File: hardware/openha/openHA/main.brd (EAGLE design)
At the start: 20 x 20 mm, 58 parts, among them U1 STM32L476JX, U2 PCM1774RGPR, U3 STC3115IQT, X1 ABS06-107SMT, X2 ABS06-107SMT

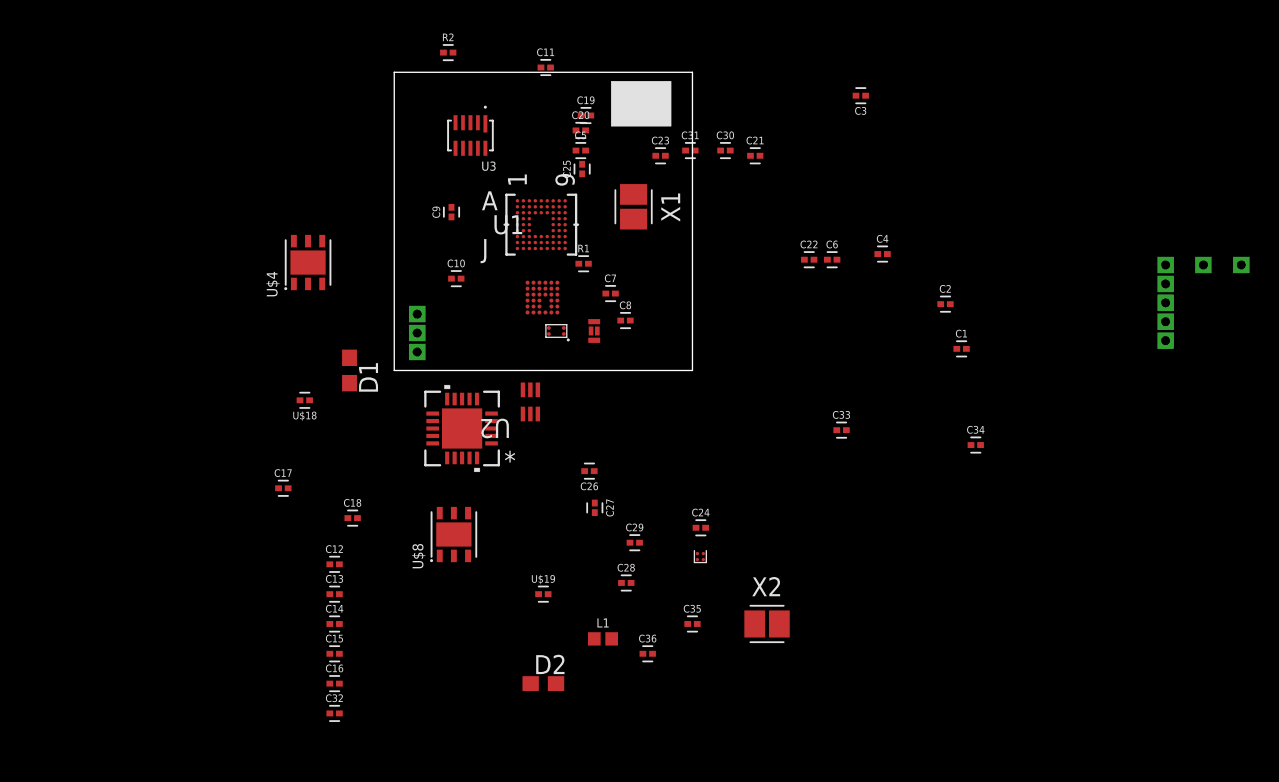
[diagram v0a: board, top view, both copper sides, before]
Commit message: Initial corrections
Miscellaneous corrections of the initial commit
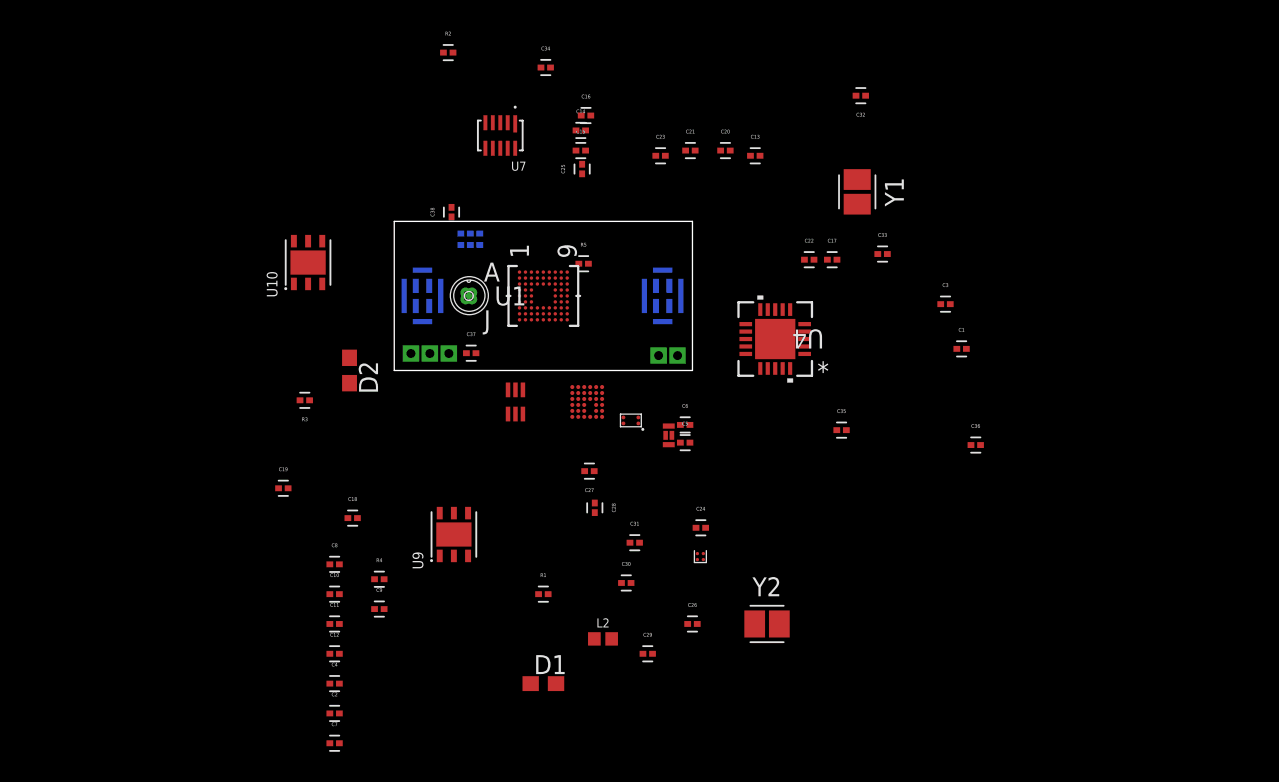
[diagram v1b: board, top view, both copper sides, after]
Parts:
- removed U$1: BATT, STM32:BATCONN
- removed U$15: BLUENRG-MS, STM32:WLCSP34
- removed U$16: BALF-NRG-01D3, STM32:FLIPCHIP
- removed U$17: ANT, STM32:ANTPACK
- removed U$18, U$19: 2k, STM32:CAPC0603X30
- removed U$2: USB, STM32:USB-MICRO-DUMMY
- removed U$3: LD5115J18, STM32:FLIPCHIP-2
- removed U$4: STBC08, STM32:DFN6
- removed U$5: USBLC6-2, STM32:SOT-666
- removed U$7: MP34DT05-A, STM32:MIC-PACK
- removed U$8: LDK130, STM32:DFN6
- removed X1, X2: ABS06-107SMT, STM32:CAPC2215X70
- added A1: ANT, OAlib:ANTPACK
- added C37, C38: 4.7uF, OAlib:CAPC0603X30
- added J1: 2PIN, OAlib:2PINCON
- added J2: BATT, OAlib:BATCONN
- added J3: CS44, OAlib:CS44
- added L2: 3.9NH, SparkFun-Coils:0402
- added R3: 2k, OAlib:CAPC0603X30
- added R4: 0R, OAlib:CAPC0603X30
- added R5: 20k, OAlib:CAPC0603X30
- added S2: SW_DPDT, OAlib:SW_DPDT
- added U10: STBC08, OAlib:DFN6
- added U4: PCM1774RGPR, PCM1774:RGP20_2P7X2P7
- added U5: BLUENRG-MS, OAlib:WLCSP34
- added U6: LD39115J18, OAlib:FLIPCHIP-2
- added U7: STC3115IQT, STC3115IQT:SON50P300X200X60-10N
- added U8: USBLC6-2, OAlib:SOT-666
- added U9: LDK130, OAlib:DFN6
- added Y1, Y2: ABS06-107SMT, OAlib:CAPC2215X70
- C1, C11, C12, C17, C18, C19, C21, C22, C23, C24, C25, C3, C7, C8, R2: device STM32:CAPC0603X30 -> OAlib:CAPC0603X30
- C10, C34, C6, C9: value 4.7uF -> 1uF; device STM32:CAPC0603X30 -> OAlib:CAPC0603X30
- C13: value 1uF -> 100nF; device STM32:CAPC0603X30 -> OAlib:CAPC0603X30
- C14, C15, C16: value 1uF -> 4.7uF; device STM32:CAPC0603X30 -> OAlib:CAPC0603X30
- C2: value 4pF -> 1uF; device STM32:CAPC0603X30 -> OAlib:CAPC0603X30
- C20: value 4.7uF -> 100pF; device STM32:CAPC0603X30 -> OAlib:CAPC0603X30
- C26: value 150nF -> 15pF; device STM32:CAPC0603X30 -> OAlib:CAPC0603X30
- C27: value 100p -> 150nF; device STM32:CAPC0603X30 -> OAlib:CAPC0603X30
- C28: value 100nF -> 100p; device STM32:CAPC0603X30 -> OAlib:CAPC0603X30
- C29: value 1uF -> 15pF; device STM32:CAPC0603X30 -> OAlib:CAPC0603X30
- C30: value 100pF -> 100nF; device STM32:CAPC0603X30 -> OAlib:CAPC0603X30
- C31, C4: value 100nF -> 1uF; device STM32:CAPC0603X30 -> OAlib:CAPC0603X30
- C32: value 1uF -> 4pF; device STM32:CAPC0603X30 -> OAlib:CAPC0603X30
- C33, C5: value 4.7uF -> 100nF; device STM32:CAPC0603X30 -> OAlib:CAPC0603X30
- C35, C36: value 15pF -> 4.7uF; device STM32:CAPC0603X30 -> OAlib:CAPC0603X30
- L1: value 3.9NH -> BALF-NRG-01D3; device SparkFun-Coils:0402 -> OAlib:FLIPCHIP
- R1: value 20k -> 2k; device STM32:CAPC0603X30 -> OAlib:CAPC0603X30
- U1: device STM32:WLCSP72 -> OAlib:WLCSP72
- U2: value PCM1774RGPR -> MP34DT05-A; device PCM1774:RGP20_2P7X2P7 -> OAlib:MIC-PACK
- U3: value STC3115IQT -> MP34DT05-A; device STC3115IQT:SON50P300X200X60-10N -> OAlib:MIC-PACK
- moved C32 54.4 mm to (31.3, 18.4), turned to 180 degrees
- moved C2 49.3 mm to (-4.00, -23.0)
- moved C4 46.7 mm to (-4.00, -21.0)
- moved C16 41.7 mm to (12.9, 17.1)
- moved C13 40.7 mm to (24.2, 14.4)
- moved C11 39.9 mm to (-4.00, -17.0)
- moved C17 39.9 mm to (29.4, 7.43)
- moved C34 38.4 mm to (10.2, 20.3)
- moved C15 37.6 mm to (12.5, 14.8)
- moved C14 37.0 mm to (12.5, 16.1)
- moved C7 35.4 mm to (-4.00, -25.0)
- moved C19 32.2 mm to (-7.44, -7.90)
- moved C30 29.8 mm to (15.6, -14.2)
- moved C9 27.1 mm to (-1.00, -16.0), turned to 0 degrees
- moved C31 26.6 mm to (16.1, -11.6)
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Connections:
- removed net GG_SCL: U3.3
- removed net GG_SDA: U1.G1, U3.2
- removed net GPIO2: U1.F8, U2.3
- removed net GPIO3: U1.F9, U2.4
- removed net MIC_CLK: U$7.CLK, U1.F7
- removed net MIC_DATA: U$7.DOUT, U1.B7
- removed net RXD-USB_DM: U$5.1
- removed net SAI_FS: U2.11
- removed net SAI_MCLK: U2.10
- removed net VDD: C12.1, C13.1, C14.1, C15.1, C16.1, C22.1, C23.1, C24.1, C25.1, C26.1, C27.1, C28.2, C29.2, C3.1, C30.1, C31.1, C32.1, C7.1, C8.1, U$15.A3, U$15.C1, U$15.D5, U$15.F3, U$3.B1, U$7.VDD, U1.A9, U1.B9, U1.G8, U1.H9, U1.J1, U1.J8
- new net 1V8: C10.1, C11.1, C12.1, C2.1, C20.1, C21.1, C22.1, C23.1, C24.1, C25.1, C27.1, C28.1, C30.2, C31.2, C32.1, C4.1, C5.1, C6.1, C7.1, C8.1, C9.1, U1.A9, U1.B9, U1.G8, U1.H9, U1.J1, U1.J8, U2.VDD, U3.VDD, U5.A3, U5.C1, U5.D5, U5.F3, U6.B1
- new net I2C_SCL: U1.F9, U4.4, U7.3
- new net I2C_SDA: U1.F8, U4.3, U7.2
- new net MIC1_CLK: U1.F7, U2.CLK
- new net MIC1_DATA: U1.B7, U2.DOUT
- new net MIC2_CLK: U1.G3, U3.CLK
- new net MIC2_DATA: U1.H3, U3.DOUT
- new net N$20: U1.D2
- new net SAI_BCK: U1.C4, U4.10
- new net SAI_LR: U1.B4, U4.11
- new net SWDCLK: S2.4, U1.B2
- new net SWDIO: S2.1, U1.C2
- new net TXD-USB_DM: U1.D1, U8.1
- new net USB_DM: S2.6, U8.6
- new net USB_DP: S2.3, U8.4
- net 3V3: now also C13.2, C14.2, C15.2, C16.2, C17.2, C36.1, R4.2, U4.1, U4.13, U4.16, U4.18, U4.6, U4.7, U9.6; no longer C19.2, C20.2, C21.2, C34.1, C5.2, C6.2, U$8.6, U2.1, U2.13, U2.16, U2.18, U2.6, U2.7
- net BAT_NTC: now also J2.2, U7.8; no longer U$1.P$2, U3.8
- net BLUE_CLK: now also U5.E1; no longer U$15.E1
- net BLUE_CS: now also U5.F2; no longer U$15.F2
- net BLUE_IRQ: now also U5.D2; no longer U$15.D2
- net BLUE_MISO: now also U5.F1; no longer U$15.F1
- net BLUE_MOSI: now also U5.E2; no longer U$15.E2
- net CHRG: now also D2.1, U10.3; no longer D1.1, U$4.3
- net GND: now also A1.RADIATOR, C11.2, C13.1, C14.1, C15.1, C16.1, C17.1, C20.2, C21.2, C28.2, C36.2, C37.2, C38.2, C5.2, C6.2, D1.1, J2.3, J3.GND, L1.A2, L2.2, R5.2, U10.4, U10.7, U2.GND, U2.GND1, U2.GND2, U2.GND3, U2.LR, U3.GND, U3.GND1, U3.GND2, U3.GND3, U3.LR, U4.12, U4.17, U4.2, U4.21, U4.8, U5.A1, U5.A2, U5.A4, U5.A5, U5.B1, U5.B2, U5.B3, U5.B4, U5.B5, U5.C2, U5.C3, U5.D3, U5.D4, U5.E3, U5.F4, U6.A1, U7.5, U8.2, U9.2; no longer C13.2, C14.2, C15.2, C16.2, C19.1, C20.1, C21.1, C30.2, C31.2, C34.2, C5.1, C6.1, D2.1, L1.2, R1.2, U$1.P$3, U$15.A1, U$15.A2, U$15.A4, U$15.A5, U$15.B1, U$15.B2, U$15.B3, U$15.B4, U$15.B5, U$15.C2, U$15.C3, U$15.D3, U$15.D4, U$15.E3, U$15.F4, U$16.A2, U$17.RADIATOR, U$2.P$6, U$2.P$7, U$3.A1, U$4.4, U$5.2, U$7.GND, U$7.GND1, U$7.GND2, U$7.GND3, U$7.LR, U$8.2, U2.12, U2.17, U2.2, U2.21, U2.8, U3.5
- net HPL: now also J1.1
- net HPR: now also C19.2, J1.2; no longer C17.2
- net N$1: now also R1.1, U1.A7; no longer U$19.1, U1.A6
- net N$10: now also C19.1, U4.14; no longer C17.1, U2.14
- net N$11: now also J3.3, S2.2; no longer U$2.P$3, U$5.4
- net N$12: now also A1.FEED, L1.A1; no longer U$16.A1, U$17.FEED
- net N$13: now also L1.B1, U5.C6; no longer U$15.C6, U$16.B1
- net N$14: now also L1.B2, U5.D6; no longer U$15.D6, U$16.B2
- net N$15: now also D1.2, R1.2; no longer D2.2, U$19.2
- net N$19: now also C30.1, C31.1, U5.F5; no longer C28.1, C29.1, U$15.F5
- net N$2: now also C29.2, L2.1; no longer C36.2, L1.1
- net N$3: now also U4.15; no longer U2.15
- net N$6: now also D2.2, R3.2; no longer D1.2, U$18.2
- net N$7: now also C34.2, U7.6; no longer C11.2, U3.6
- net N$8: now also R5.1, U10.5; no longer R1.1, U$4.5
- net N$9: now also J3.2, S2.5; no longer U$2.P$2, U$5.6
- net OSC_BLUE_IN: now also C26.1, U5.A6, Y2.1; no longer C35.1, U$15.A6, X2.1
- net OSC_BLUE_OUT: now also C29.1, U5.B6, Y2.2; no longer C36.1, U$15.B6, X2.2
- net OSC_IN: now also Y1.1; no longer X1.1
- net OSC_OUT: now also C3.1, Y1.2; no longer C2.1, X1.2
- net RESETN: now also U5.E4; no longer U$15.E4
- net RXD-USB_DP: now also U1.C1, U8.3; no longer U$5.3
- net SAI_SCK: now also U1.A4, U4.9; no longer U2.9
- net SAI_SD: now also U1.C5, U4.5; no longer U2.5
- net SMPSFILT1: now also U5.F6; no longer U$15.F6
- net SXTAL0: now also U5.E5; no longer U$15.E5
- net SXTAL1: now also U5.E6; no longer U$15.E6
- net TEST1: now also U5.D1; no longer U$15.D1
- net VBAT: now also C34.1, C35.1, C38.1, J2.1, U10.1, U6.A2, U6.B2, U7.10, U7.9, U9.1; no longer C11.1, C33.1, C9.1, U$1.P$1, U$3.A2, U$3.B2, U$4.1, U$8.1, U3.10, U3.9
- net VDDUSB: now also R4.1
- net V_USB: now also C33.1, C37.1, J3.VCC, R3.1, U10.6, U8.5; no longer C10.1, C4.1, U$18.1, U$2.P$1, U$4.6, U$5.5
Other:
- board size 20 x 20 mm -> 20 x 10 mm

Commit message: Various BOM update
Replace 4pin micro connector by USB (used for USB and SWD)
Update BOM for LED, Crystal, Self and 3V3 LDO
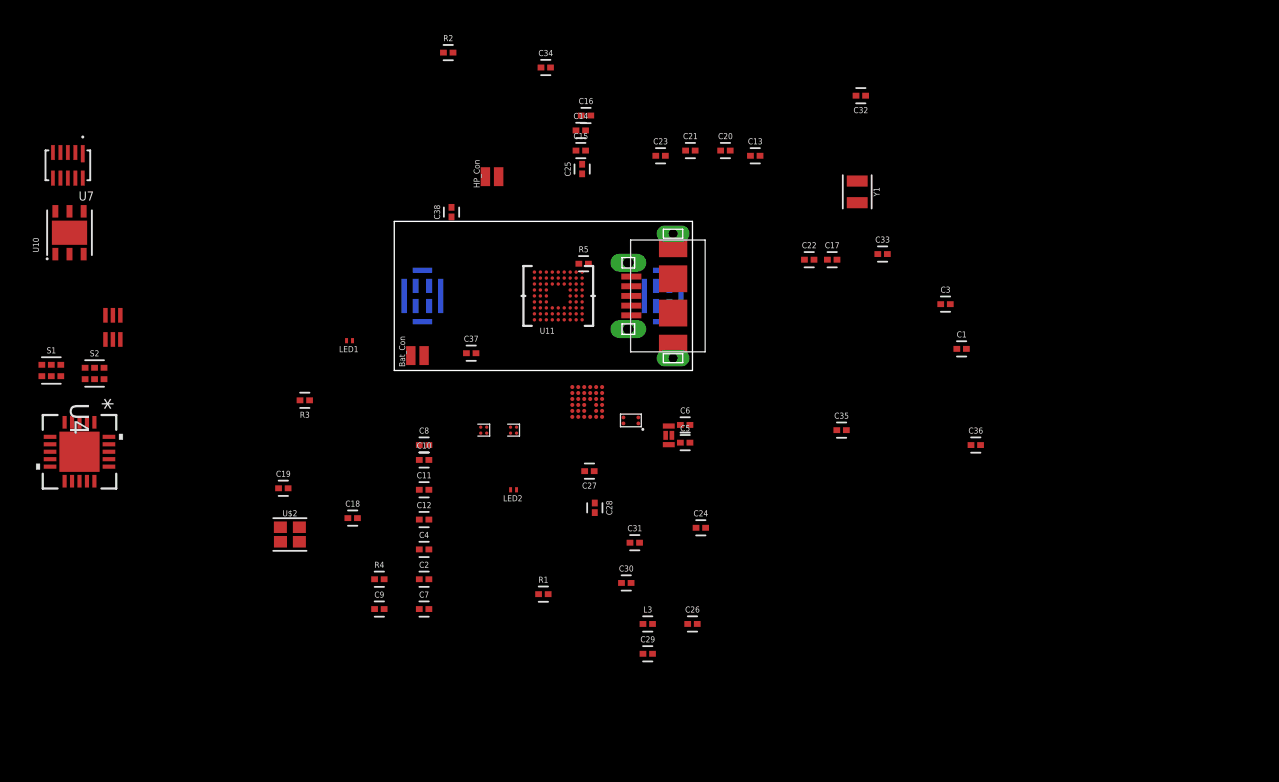
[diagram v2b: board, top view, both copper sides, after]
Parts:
- removed D1, D2: LTST-C191KSKT, LTST-C191KSKT:0603
- removed J2: BATT, OAlib:BATCONN
- removed L2: 3.9NH, SparkFun-Coils:0402
- removed U1: STM32L476JX, OAlib:WLCSP72
- removed Y2: ABS06-107SMT, OAlib:CAPC2215X70
- added L3: 3.9nH, OAlib:CAPC0603X30
- added LED1, LED2: (no value), OAlib:0.65X0.35X0.2MM(0201)SMDCHIPLE
- added S1: SW_DPDT, OAlib:SW_DPDT
- added U$1: MICRO-USB-RECEPTACLE47589-0001, OAlib:47589-0001
- added U$2: 32MHz, OAlib:ABM11W-101
- added U11: STM32L476JX, OAlib:WLCSP72
- J1: value 2PIN -> HP_Con
- J3: value CS44 -> Bat_Con; device OAlib:CS44 -> OAlib:2PINCON
- R2: value 50m -> 50M
- U6: value LD39115J18 -> LD39115J
- U9: value LDK130 -> LD39115J; device OAlib:DFN6 -> OAlib:FLIPCHIP-2
- Y1: value ABS06-107SMT -> 32.768kHz; device OAlib:CAPC2215X70 -> OAlib:ABS06-107
- moved U4 47.3 mm to (-21.1, -5.45), turned to 270 degrees
- moved U7 29.1 mm to (-21.9, 13.8)
- moved U8 27.5 mm to (-18.9, 2.89)
- moved S2 26.8 mm to (-20.1, -0.20), flipped to the top
- moved J1 17.0 mm to (7.00, 13.0)
- moved U6 16.8 mm to (6.00, -4.00), turned to 0 degrees
- moved U10 16.1 mm to (-21.8, 9.24)
- moved C10 10.8 mm to (2.00, -6.00)
- moved C11 10.8 mm to (2.00, -8.00)
- moved C12 10.8 mm to (2.00, -10.0)
- moved C2 10.8 mm to (2.00, -14.0)
- moved C4 10.8 mm to (2.00, -12.0)
- moved C7 10.8 mm to (2.00, -16.0)
- moved C8 10.0 mm to (2.00, -5.00)
- moved U9 8.06 mm to (8.00, -4.00), turned to 0 degrees
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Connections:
- removed net BAT_NTC: J2.2, U7.8
- new net N$16: S1.5, U$1.4
- new net SWDRST: S1.6, U11.E9
- net 1V8: now also U11.A9, U11.B9, U11.G8, U11.H9, U11.J1, U11.J8; no longer U1.A9, U1.B9, U1.G8, U1.H9, U1.J1, U1.J8
- net 3V3: now also U9.B1; no longer U9.6
- net BLUE_CLK: now also U11.H6; no longer U1.H6
- net BLUE_CS: now also U11.J3; no longer U1.J3
- net BLUE_IRQ: now also U11.J6; no longer U1.J6
- net BLUE_MISO: now also U11.H5; no longer U1.H5
- net BLUE_MOSI: now also U11.H4; no longer U1.H4
- net BLUE_RST: now also U11.D9; no longer U1.D9
- net CHRG: now also LED1.1; no longer D2.1
- net GND: now also J3.P$2, L3.2, LED2.1, U$1.5, U$2.2, U$2.4, U11.A8, U11.B1, U11.D7, U11.G9, U11.J2, U11.J9, U9.A1; no longer D1.1, J2.3, J3.GND, L2.2, U1.A8, U1.B1, U1.D7, U1.G9, U1.J2, U1.J9, U9.2
- net HPL: now also J1.P$1; no longer J1.1
- net HPR: now also J1.P$2; no longer J1.2
- net I2C_SCL: now also U11.F9; no longer U1.F9
- net I2C_SDA: now also U11.F8; no longer U1.F8
- net MIC1_CLK: now also U11.F7; no longer U1.F7
- net MIC1_DATA: now also U11.B7; no longer U1.B7
- net MIC2_CLK: now also U11.G3; no longer U1.G3
- net MIC2_DATA: now also U11.H3; no longer U1.H3
- net N$1: now also U11.A7; no longer U1.A7
- net N$11: now also U$1.3; no longer J3.3
- net N$15: now also LED2.2; no longer D1.2
- net N$2: now also L3.1; no longer L2.1
- net N$20: now also U11.D2; no longer U1.D2
- net N$6: now also LED1.2; no longer D2.2
- net N$9: now also U$1.2; no longer J3.2
- net OSC_BLUE_IN: now also U$2.1; no longer Y2.1
- net OSC_BLUE_OUT: now also U$2.3; no longer Y2.2
- net OSC_IN: now also U11.C9; no longer U1.C9
- net OSC_OUT: now also U11.C8; no longer U1.C8
- net RXD-USB_DP: now also U11.C1; no longer U1.C1
- net SAI_BCK: now also U11.C4; no longer U1.C4
- net SAI_LR: now also U11.B4; no longer U1.B4
- net SAI_SCK: now also U11.A4; no longer U1.A4
- net SAI_SD: now also U11.C5; no longer U1.C5
- net SWDCLK: now also U11.B2; no longer U1.B2
- net SWDIO: now also U11.C2; no longer U1.C2
- net TXD-USB_DM: now also U11.D1; no longer U1.D1
- net VBAT: now also J3.P$1, U9.A2, U9.B2; no longer J2.1, U9.1
- net VDDUSB: now also U11.A1, U11.B6; no longer U1.A1, U1.B6
- net V_USB: now also U$1.1; no longer J3.VCC
